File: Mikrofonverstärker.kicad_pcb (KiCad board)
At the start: 2 copper layers, 60 parts, among them J1 Screw_Terminal_01x02, J3 Screw_Terminal_01x02, J4 Screw_Terminal_01x03, J5 USB_C_Receptacle_USB2.0_14P, U1 CM108B, U2 THAT151xx08, U3 NMA0515SC

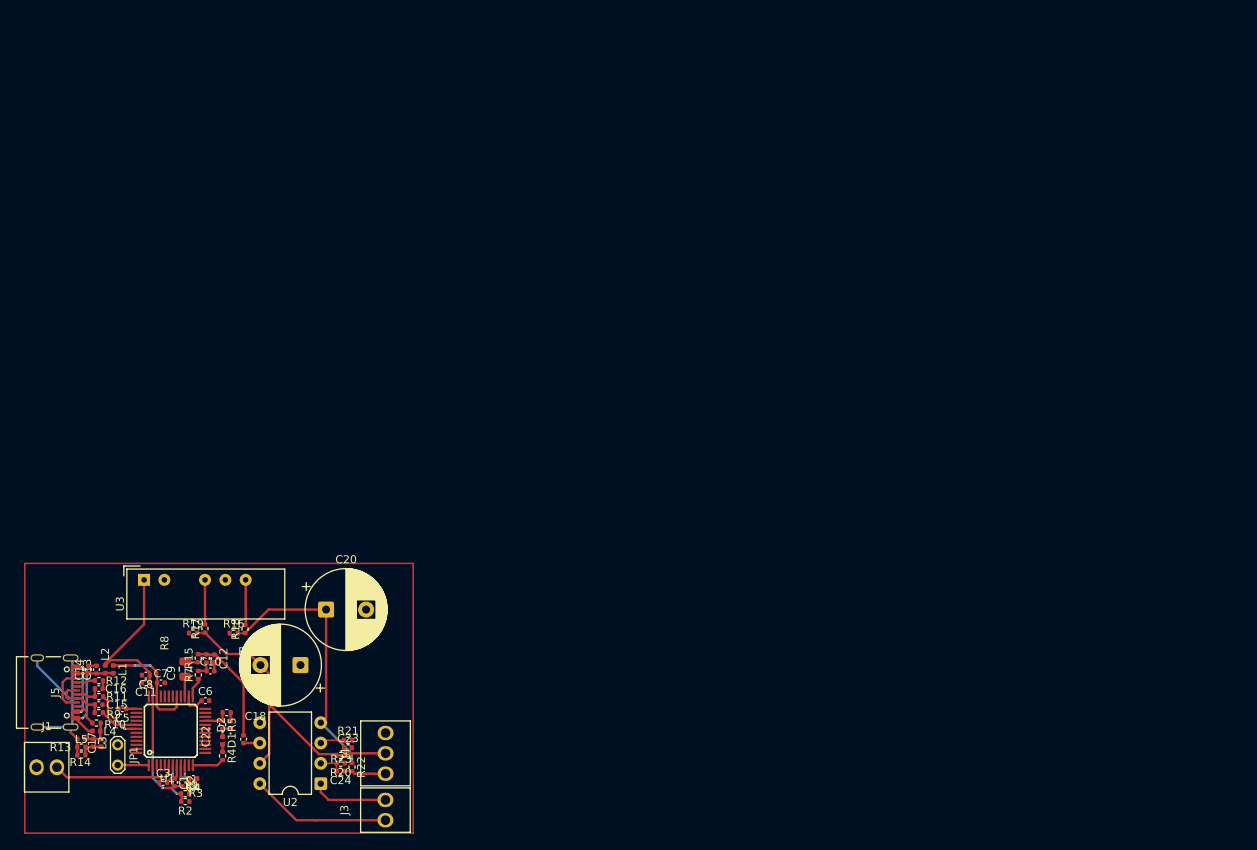
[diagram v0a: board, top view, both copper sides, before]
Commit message: autorouting ausprobiert
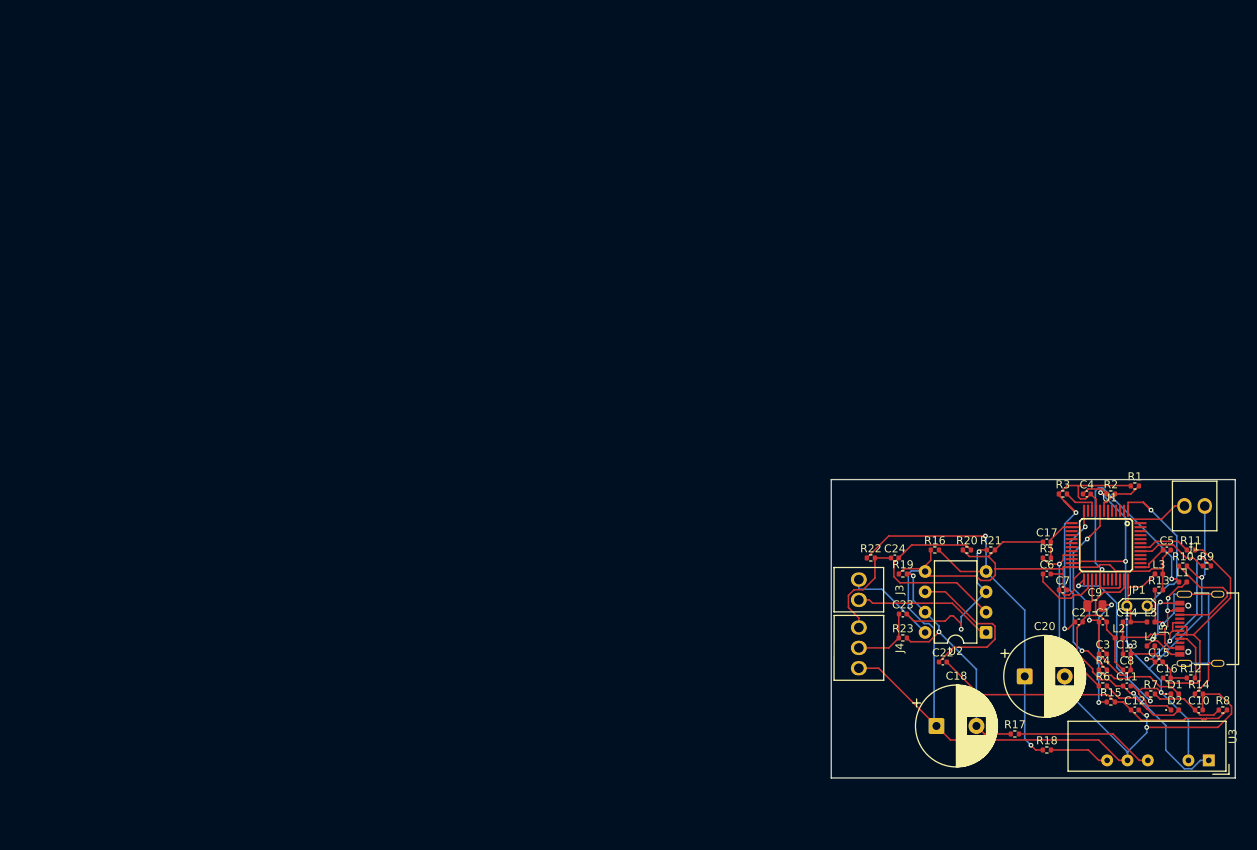
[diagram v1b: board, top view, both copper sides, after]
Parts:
- moved J1 147.2 mm to (217.2, 107.7), turned to 0 degrees
- moved J5 143.3 mm to (217.8, 123.0), turned to 90 degrees
- moved R14 139.9 mm to (217.7, 131.2)
- moved R9 139.7 mm to (218.7, 115.2), turned to 0 degrees
- moved R11 137.7 mm to (216.7, 113.2), turned to 0 degrees
- moved R10 137.2 mm to (215.7, 115.2)
- moved R12 136.5 mm to (216.7, 129.2), turned to 0 degrees
- moved R13 136.1 mm to (212.7, 118.2)
- moved U3 135.0 mm to (218.9, 139.5), turned to -90 degrees
- moved L3 134.9 mm to (212.7, 116.2), turned to 0 degrees
- moved L5 134.5 mm to (211.7, 122.2), turned to 0 degrees
- moved L1 134.1 mm to (215.7, 117.2), turned to 0 degrees
- moved C16 133.5 mm to (213.7, 129.2)
- moved C15 132.6 mm to (212.7, 127.2)
- moved L4 132.2 mm to (211.7, 125.2)
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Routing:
- net GNDA: track 4.09 -> 162.9 mm, vias 0 -> 2
- net GNDD: track 8.21 -> 126.8 mm, vias 0 -> 5
- net Net-(C2-Pad1): track 4.54 -> 43.5 mm, vias 0 -> 2
- net VAA: track 14.2 -> 40.6 mm
- net AMICIN: track 13.7 -> 39.5 mm
- net Net-(C16-Pad1): track 5.45 -> 29.6 mm
- net Net-(U2--In): track 3.04 -> 25.9 mm
- net Net-(JP1-B): track 3.91 -> 25.0 mm, vias 0 -> 1
- net Net-(C1-Pad1): track 2.93 -> 23.8 mm, vias 0 -> 2
- net Net-(U2-V-): track 33.3 -> 53.2 mm, vias 1 -> 2
- net Net-(R4-Pad2): track 3.99 -> 23.4 mm, vias 0 -> 2
- net Net-(R7-Pad1): track 2.59 -> 21.8 mm, vias 0 -> 2
- net Net-(R5-Pad1): track 3.18 -> 22.0 mm, vias 0 -> 2
- net Net-(U2-Out): track 3.58 -> 20.3 mm
- net Net-(U2-+In): track 4.53 -> 21.1 mm, vias 0 -> 2
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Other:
- board outline added: 50.5 x 37.3 mm

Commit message: schaltung ist fertig maschalla
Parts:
- C22, C23, C24: footprint Capacitor_SMD:C_0402_1005Metric -> Capacitor_SMD:C_0805_2012Metric
- R16, R17, R18, R19, R20, R21, R22, R23: footprint Resistor_SMD:R_0402_1005Metric -> Resistor_SMD:R_0805_2012Metric
- moved U3 81.6 mm to (147.6, 100.0), turned to 90 degrees
- moved R14 79.9 mm to (145.8, 96.3)
- moved J5 77.8 mm to (147.6, 89.5), turned to -90 degrees
- moved R12 76.1 mm to (152.6, 88.2), turned to 180 degrees
- moved C16 71.1 mm to (155.3, 88.6), turned to 90 degrees
- moved R13 70.7 mm to (145.8, 95.3)
- moved L5 69.5 mm to (146.7, 97.5), turned to 180 degrees
- moved D1 69.1 mm to (160.7, 88.0)
- moved D2 68.4 mm to (160.7, 91.2)
- moved L3 68.3 mm to (147.7, 95.3), turned to 180 degrees
- moved C15 68.1 mm to (155.3, 90.6), turned to -90 degrees
- moved L4 67.8 mm to (151.8, 93.3), turned to -90 degrees
- moved R10 67.5 mm to (152.7, 91.0)
- moved R9 66.8 mm to (156.8, 90.1), turned to 180 degrees
- moved L1 65.3 mm to (155.2, 92.5), turned to 90 degrees
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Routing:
- net GNDA: track 162.9 -> 18.8 mm, vias 2 -> 11
- net GNDD: track 126.8 -> 20.6 mm, vias 5 -> 18
- net Net-(C2-Pad1): track 43.5 -> 5.21 mm, vias 2 -> 0
- net AMICIN: track 39.5 -> 4.85 mm
- net GNDPWR: track 35.9 -> 4.65 mm, vias 1 -> 0
- net Net-(U2--In): track 25.9 -> 4.34 mm
- net Net-(C16-Pad1): track 29.6 -> 8.10 mm
- net Net-(JP1-B): track 25.0 -> 4.16 mm, vias 1 -> 0
- net Net-(R7-Pad1): track 21.8 -> 1.81 mm, vias 2 -> 0
- net Net-(R5-Pad1): track 22.0 -> 3.80 mm, vias 2 -> 0
- net Net-(U2-Out): track 20.3 -> 2.62 mm
- net VAA: track 40.6 -> 23.1 mm
- net Net-(R4-Pad2): track 23.4 -> 6.17 mm
- net Net-(U2-+In): track 21.1 -> 4.22 mm, vias 2 -> 0
- net Net-(U2-V-): track 53.2 -> 37.3 mm, vias 2 -> 0
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- added copper zone on B.Cu, net GNDA
- added copper zone on B.Cu, net GNDD
- added copper zone on B.Cu, net GNDPWR
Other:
- board size 50.5 x 37.3 mm -> 47.8 x 39.7 mm

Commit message: final layout
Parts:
- moved L3 9.03 mm to (156.7, 96.2), turned to -90 degrees
- moved R13 8.51 mm to (154.2, 96.6), turned to -90 degrees
- moved C17 7.88 mm to (155.6, 96.2), turned to 90 degrees
- moved R14 7.42 mm to (153.2, 96.6), turned to -90 degrees
- moved L5 6.77 mm to (153.1, 95.2)
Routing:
- net GNDPWR: track 4.65 -> 8.09 mm, vias 0 -> 1
- net GNDA: track 18.8 -> 16.0 mm, vias 11 -> 17
- net VDD: track 57.4 -> 59.5 mm
- net GNDD: track 20.6 -> 22.2 mm, vias 18 -> 20
- net Net-(J3-Pin_1): track 11.0 -> 11.8 mm
- added copper zone on F.Cu, net GNDA
- added copper zone on F.Cu, net GNDD
- added copper zone on F.Cu, net GNDPWR

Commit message: almost perfection
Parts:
- moved C1 73.7 mm to (110.3, 49.3)
- moved C10 73.7 mm to (102.5, 63.1)
- moved C15 73.7 mm to (90.2, 56.0)
- moved C16 73.7 mm to (90.2, 54.1)
- moved C2 73.7 mm to (101.6, 48.9)
- moved C22 73.7 mm to (102.0, 71.0)
- moved C4 73.7 mm to (103.5, 47.9)
- moved C5 73.7 mm to (111.7, 58.7)
- moved C6 73.7 mm to (103.0, 61.7)
- moved D1 73.7 mm to (95.6, 53.5)
- moved D2 73.7 mm to (95.6, 56.6)
- moved J1 73.7 mm to (122.2, 60.7)
- moved J3 73.7 mm to (122.2, 77.0)
- moved JP1 73.7 mm to (114.7, 51.0)
- moved L1 73.7 mm to (90.1, 58.0)
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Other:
- board text added: "MUTE"
- board text added: "PWR"

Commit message: fertiges projekt
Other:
- board text added: "GAIN"
- board text added: "MIC"
- board text added: "MUTE SWITCH"
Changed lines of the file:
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@@
 		(layer "Edge.Cuts")
+	)
+	(gr_text "MUTE\nSWITCH"
+		(at 116.4 58.6 0)
+		(layer "F.SilkS")
+		(effects
+			(font
+				(size 0.4 0.4)
+				(thickness 0.05)
+			)
+			(justify left bottom)
+		)
+	)
+	(gr_text "GAIN"
+		(at 117.6 76.2 0)
+		(layer "F.SilkS")
+		(effects
+			(font
+				(size 0.4 0.4)
+				(thickness 0.05)
+			)
+			(justify left bottom)
+		)
 	)
 	(gr_text "MUTE"
@@
 		(layer "F.SilkS")
 		(effects
+			(font
+				(size 0.4 0.4)
+				(thickness 0.05)
+			)
+			(justify left bottom)
+		)
+	)
+	(gr_text "MIC"
+		(at 117.4 66.5 0)
+		(layer "F.SilkS")
+		(effects
